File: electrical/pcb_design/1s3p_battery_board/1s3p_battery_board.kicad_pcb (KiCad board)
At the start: 4 copper layers, 82.5 x 82.5 mm, 92 parts, among them J1 STLINK, J2 Molex_504050-1291, J3 Molex_504050-1291, J4 Power Interconnect, Q1 CSD16342Q5A, Q2 CSD16342Q5A, Q3 CSD16342Q5A, U1 STM32L452RCTx, U2 TCAN330DR, U3 PAC1934T-I/JQ, U8 TPS63900

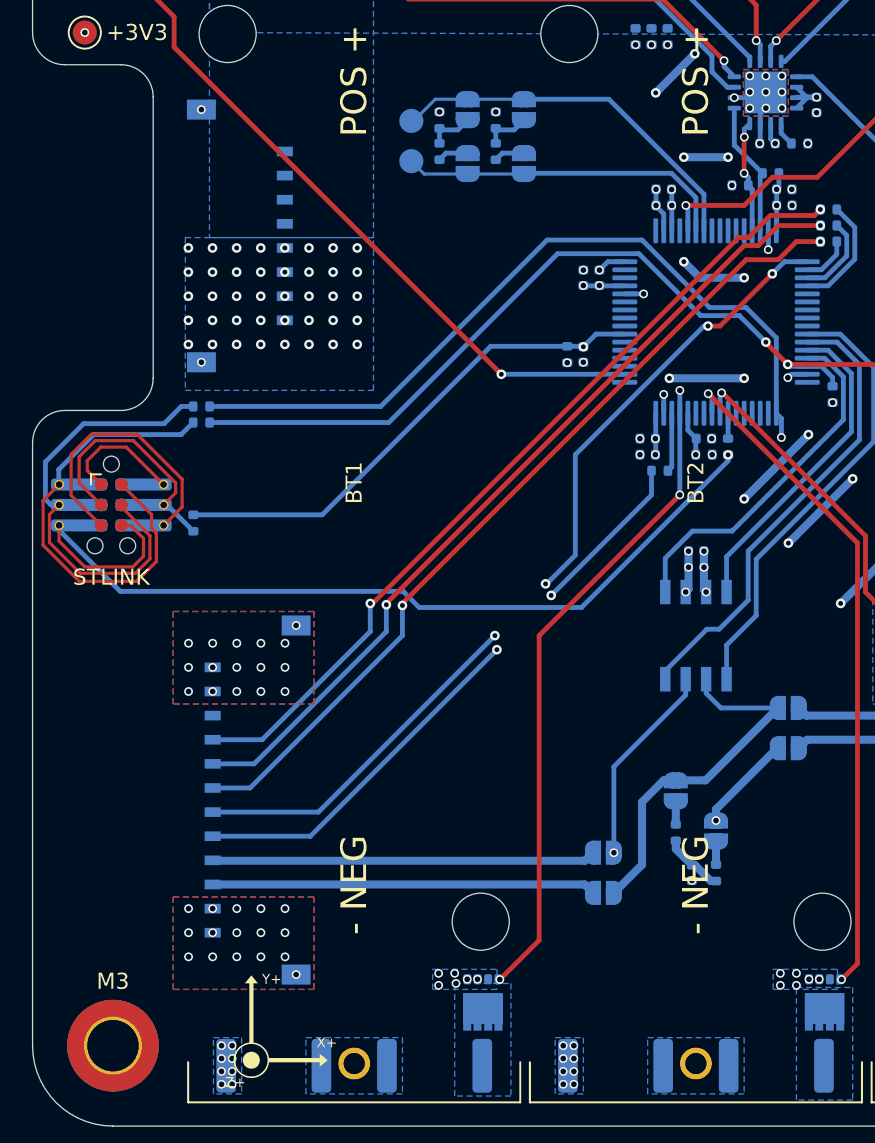
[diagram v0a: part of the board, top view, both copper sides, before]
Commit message: Update layout of battery board with new PCB and TagConnect footprints. This new layout makes the cable channel on the left (negative X) match the cable channels on other boards.
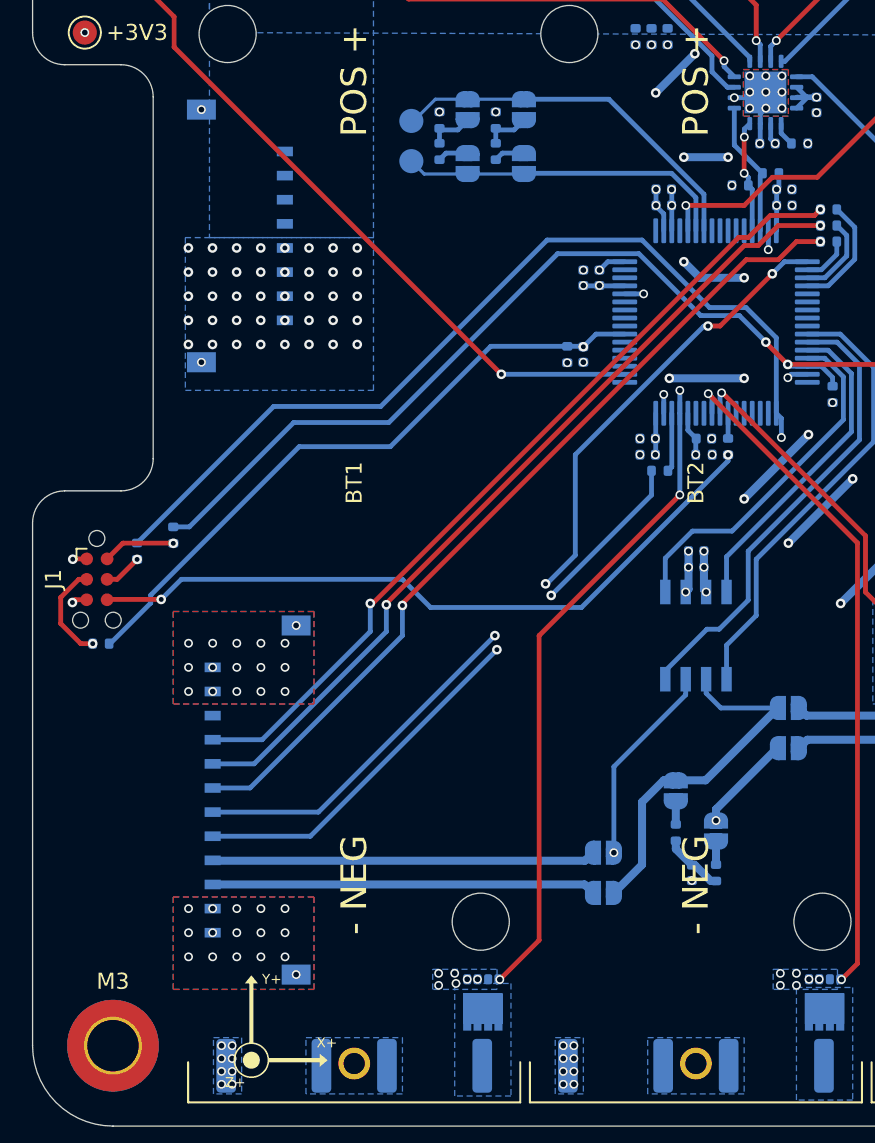
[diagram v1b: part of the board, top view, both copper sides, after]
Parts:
- J1: footprint footprints:Double-Sided_Tag-Connect_TC2030-IDC-NL_2x03_P1.27mm_Vertical -> Connector:Tag-Connect_TC2030-IDC-NL_2x03_P1.27mm_Vertical; moved to F.Cu
- moved R39 9.85 mm to (121.2, 110.4), turned to -90 degrees
- moved R37 9.45 mm to (119.0, 116.2), turned to 180 degrees
- moved R38 7.22 mm to (123.5, 109.4), turned to -90 degrees
- moved J1 4.71 mm to (118.7, 112.2)
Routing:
- net Net-(J1-T_SWCLK): track 27.9 -> 2.38 mm, vias 0 -> 1
- net Net-(J1-T_SWDIO): track 28.9 -> 4.53 mm, vias 0 -> 1
- net GND: track 55.3 -> 39.1 mm, vias 164 -> 165
- net /SWO: track 86.9 -> 72.5 mm, vias 2 -> 3
- net Net-(J1-T_NRST): track 15.3 -> 6.21 mm, vias 0 -> 1
- net /NRST: track 77.1 -> 86.0 mm
- net /SWCLK: track 78.7 -> 86.8 mm
- net +3V3: track 44.7 -> 37.7 mm, vias 33 -> 34
- net /SWDIO: track 87.6 -> 92.6 mm
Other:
- outline, holes or cut-outs redrawn

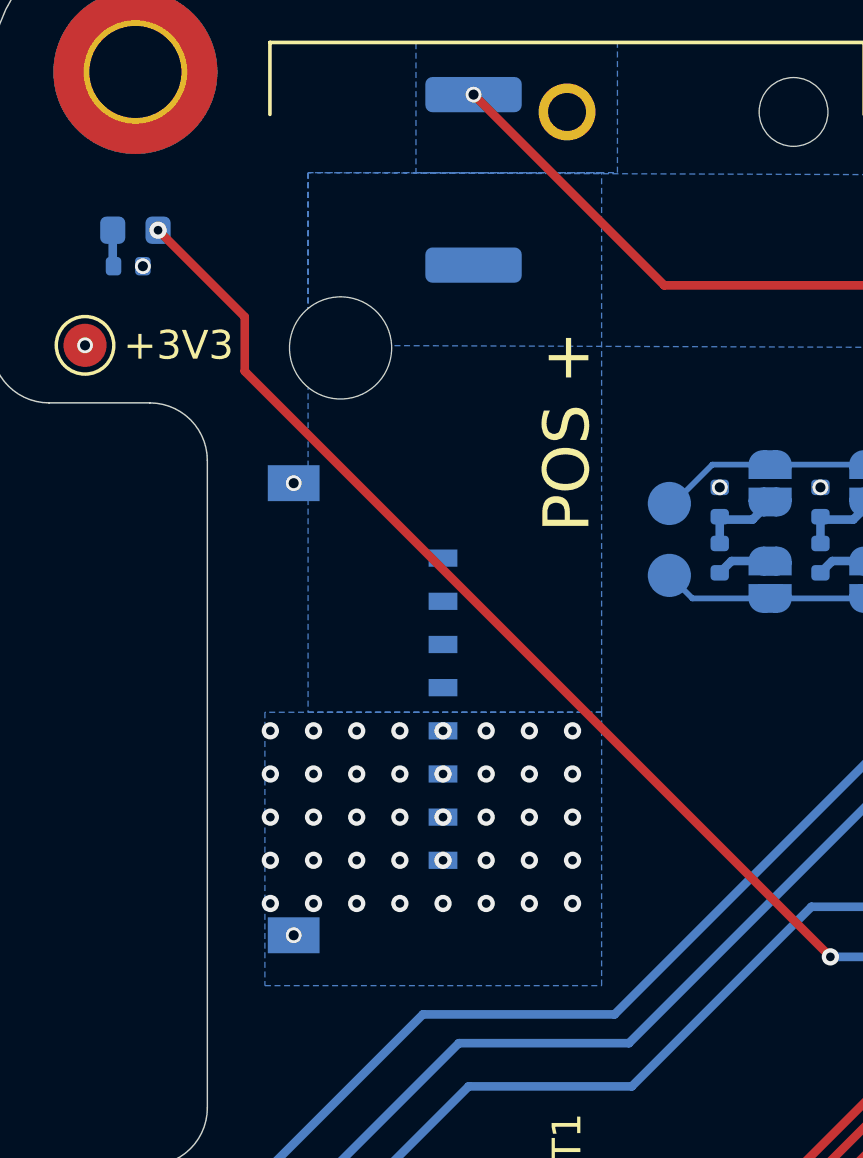
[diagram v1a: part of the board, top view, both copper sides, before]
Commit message: Substitute 6-pin Pico-Lock for primary power interconnect. The 8-pin version is not available. The 6-pin header should still allow more than 5A of current, but it does share the header and cable as the solar interconnect from the magnetorquer to the power board.
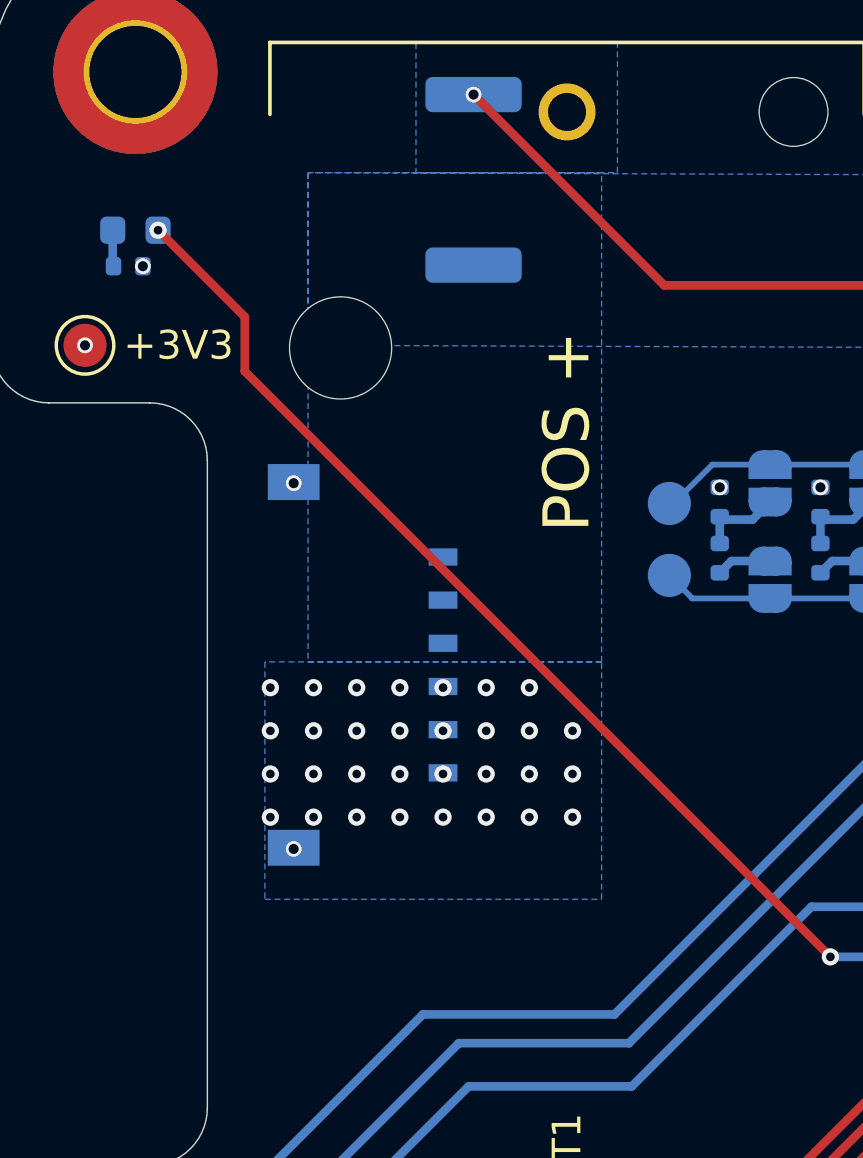
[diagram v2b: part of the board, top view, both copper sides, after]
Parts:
- J4: footprint footprints:Molex_504050-0891 -> footprints:Molex_504050-0691
- moved J4 3.04 mm to (130.4, 93.0)
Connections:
- J4 pad 4: GND -> VBATT
- J4 pad 7: VBATT -> GND
- J4 pad 8: VBATT -> GND
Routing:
- net GND: vias 165 -> 156

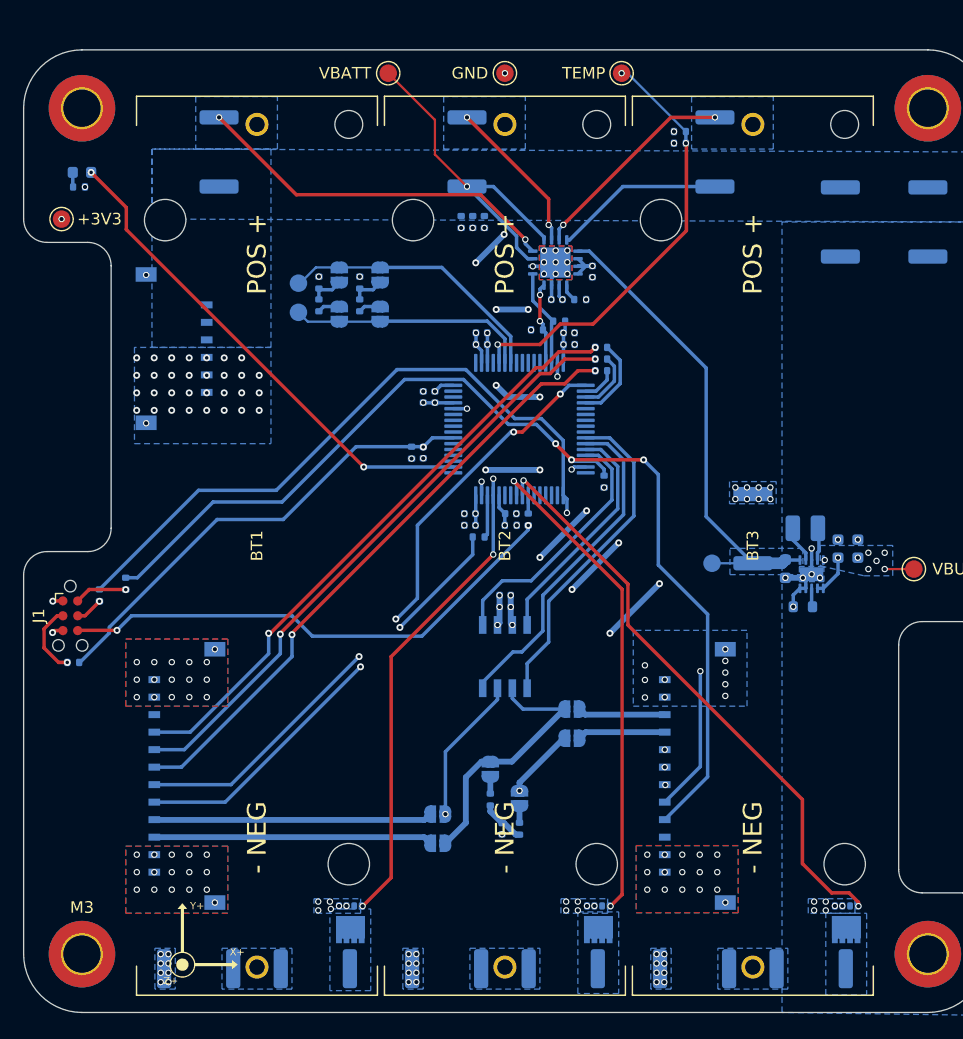
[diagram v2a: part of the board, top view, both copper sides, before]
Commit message: Change all vias to 0.3/0.5 size. Move vias off of pads.
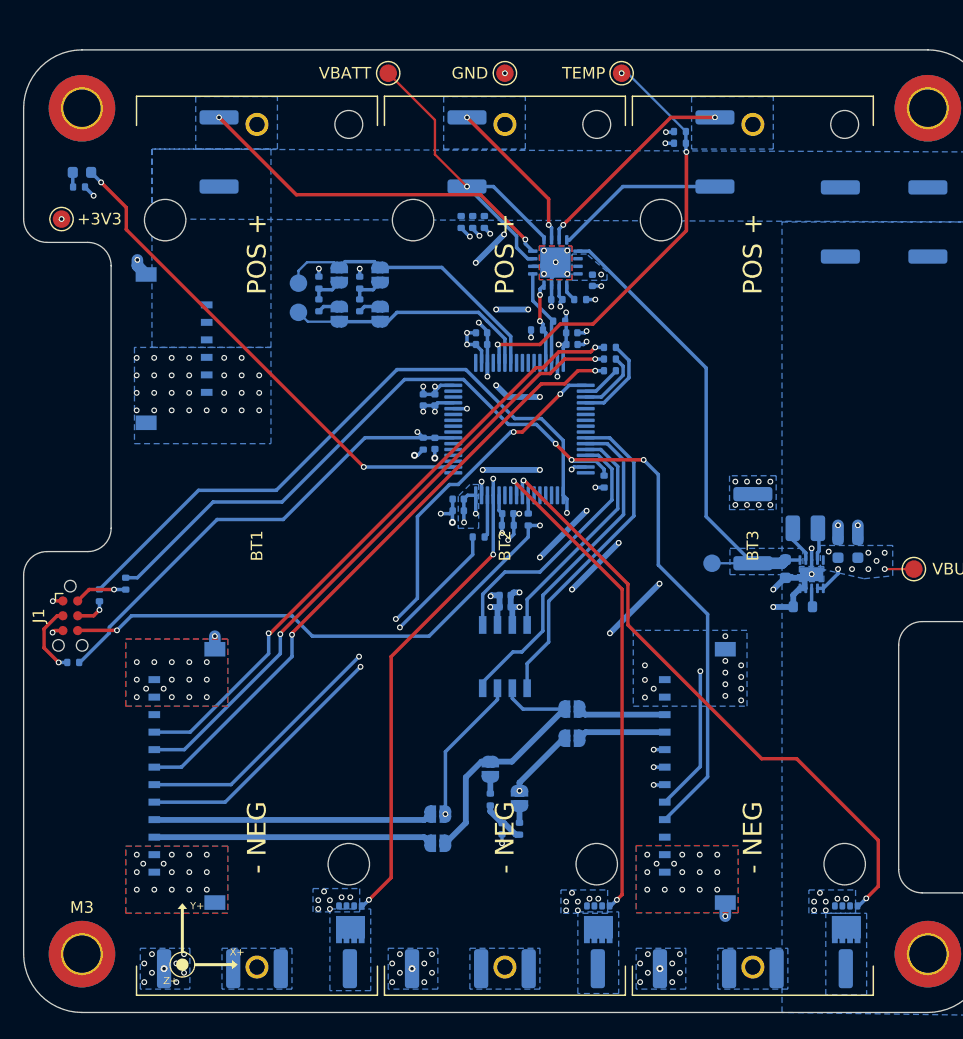
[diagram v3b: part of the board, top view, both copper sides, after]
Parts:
- moved C11 1.60 mm to (152.0, 103.2)
- moved C8 1.60 mm to (152.0, 102.2)
- moved C1 1.27 mm to (150.0, 97.4)
- moved R1 1.26 mm to (149.0, 97.4)
- moved C17 0.75 mm to (163.5, 83.4)
- moved R5 0.75 mm to (165.0, 90.2)
- moved R8 0.75 mm to (165.0, 91.2)
- moved R9 0.75 mm to (165.0, 89.2)
- moved C12 0.25 mm to (149.0, 93.7)
- moved C13 0.25 mm to (161.7, 88.9)
- moved C2 0.25 mm to (156.2, 103.4)
- moved C9 0.25 mm to (150.0, 93.7)
- moved R3 0.25 mm to (156.2, 104.4)
- moved C15 0.23 mm to (161.7, 87.9)
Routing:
- net GND: track 39.1 -> 67.6 mm, vias 156 -> 152
- net +3V3: track 37.7 -> 48.0 mm, vias 34 -> 33
- net /Batteries/BATTERY_3_EN: track 73.6 -> 76.0 mm
- net /SWO: track 72.5 -> 74.8 mm
- net /SWCLK: track 86.8 -> 88.7 mm
- net /BOOT0: track 29.8 -> 31.7 mm
- net /NRST: track 86.0 -> 87.7 mm
- net /Board Identification/BOARD_ID_SENSE: track 23.3 -> 24.9 mm
- net VBUS: track 6.15 -> 5.17 mm
- net /CTRL.SWDIO: track 52.5 -> 53.2 mm
- net /CTRL.SWCLK: track 53.0 -> 53.8 mm
- net /CTRL.NRST: track 52.7 -> 53.4 mm
- net /Board Identification/BOARD_ID_POWER: track 20.7 -> 21.4 mm
